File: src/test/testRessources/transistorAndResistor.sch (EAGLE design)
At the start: 2 parts, among them Q1 BC547

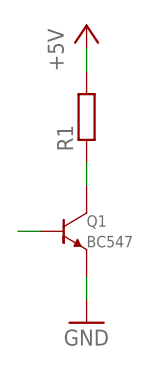
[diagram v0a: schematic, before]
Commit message: Added functional test for multiple devices
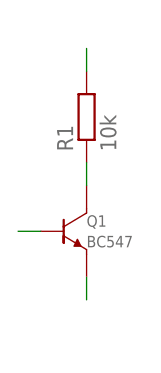
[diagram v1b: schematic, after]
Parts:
- R1: value (none) -> 10k
